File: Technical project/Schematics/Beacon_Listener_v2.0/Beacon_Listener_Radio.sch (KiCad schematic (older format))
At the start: 33 parts, among them J1 Conn_01x06_Female, J2 input AC, J3 select if usb or AC power, J4 USB_B_Micro, J5 Conn_01x03_Male, J6 Conn_01x03_Male, J7 Conn_Coaxial, SW1 SW_Push, SW2 SW_Push, U1 ESP32-WROVER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

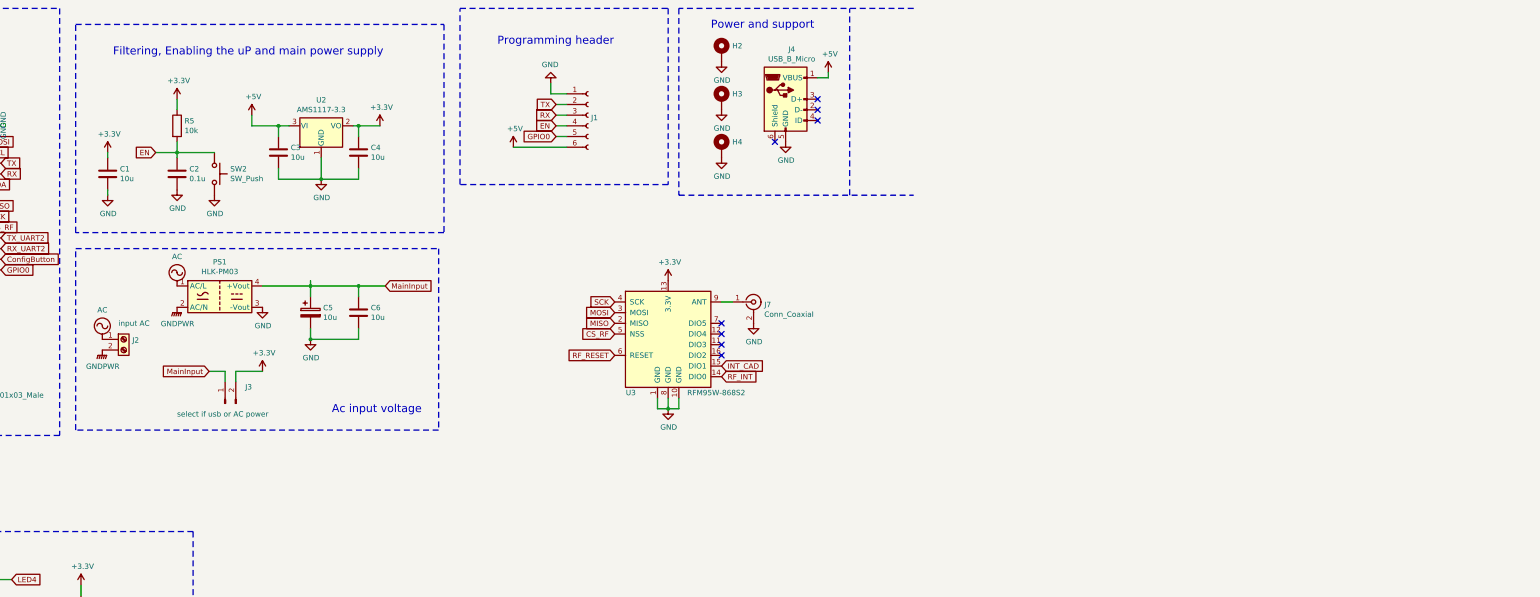
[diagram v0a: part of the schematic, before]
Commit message: rf95 module
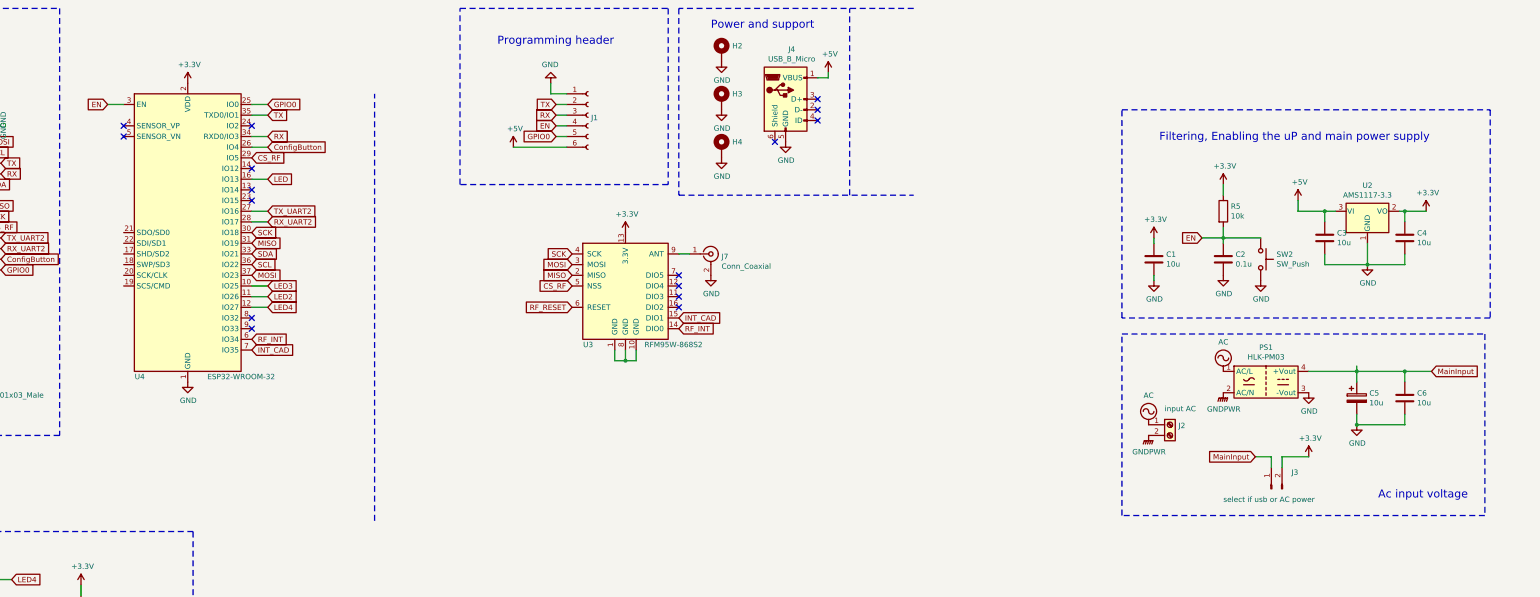
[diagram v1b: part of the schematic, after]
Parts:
- added U4: ESP32-WROOM-32, RF_Module:ESP32-WROOM-32, symbol RF_Module:ESP32-WROOM-32
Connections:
- wire segments 89 -> 100
- no-connect marks 22 -> 30
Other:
- moved on the sheet: C1, C2, C3, C4, C5, C6, J2, J3, J7, PS1, R5, SW2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

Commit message: radio module include on the 2 version of pcb
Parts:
- removed C6: 10u, Capacitor_SMD:C_0805_2012Metric_Pad1.15x1.40mm_HandSolder, symbol Device:C
- removed U1: ESP32-WROVER, ESP_32_all:ESP32-WROVER, symbol esp32_noob:ESP32-WROVER
- added C6: CP, Capacitor_Tantalum_SMD:CP_EIA-3216-10_Kemet-I, symbol Device:CP
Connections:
- wire segments 100 -> 84
- no-connect marks 30 -> 16
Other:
- moved on the sheet: C1, C2, C3, C4, C5, J2, J3, PS1, R5, SW2, U2, U4
